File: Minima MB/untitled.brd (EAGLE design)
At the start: 101.3 x 130.5 mm, 224 parts, among them IC1 78L05, IC2 78L05, K1 G5V1, K2 G5V-2, K3 G5V1, K4 G5V1, Q10 2N3904, Q11 2N3904, Q12 2N3904, Q13 2N3904, Q14 2N3904, Q15 2N3904, Q16 2N3904, Q17 BFO, Q18 J310, Q19 J310, Q20 2N3904, Q21 2N3906, Q22 2N3904, Q23 2N3904, Q24 2N3904, Q25 2N3904, Q26 2N3904, Q27 2N3904, Q28 2N3904, Q29 2N3904, Q30 2N3904, Q39 2N3904, Q8 2N3904, X1 VFO, X2 VFO, X3 PA

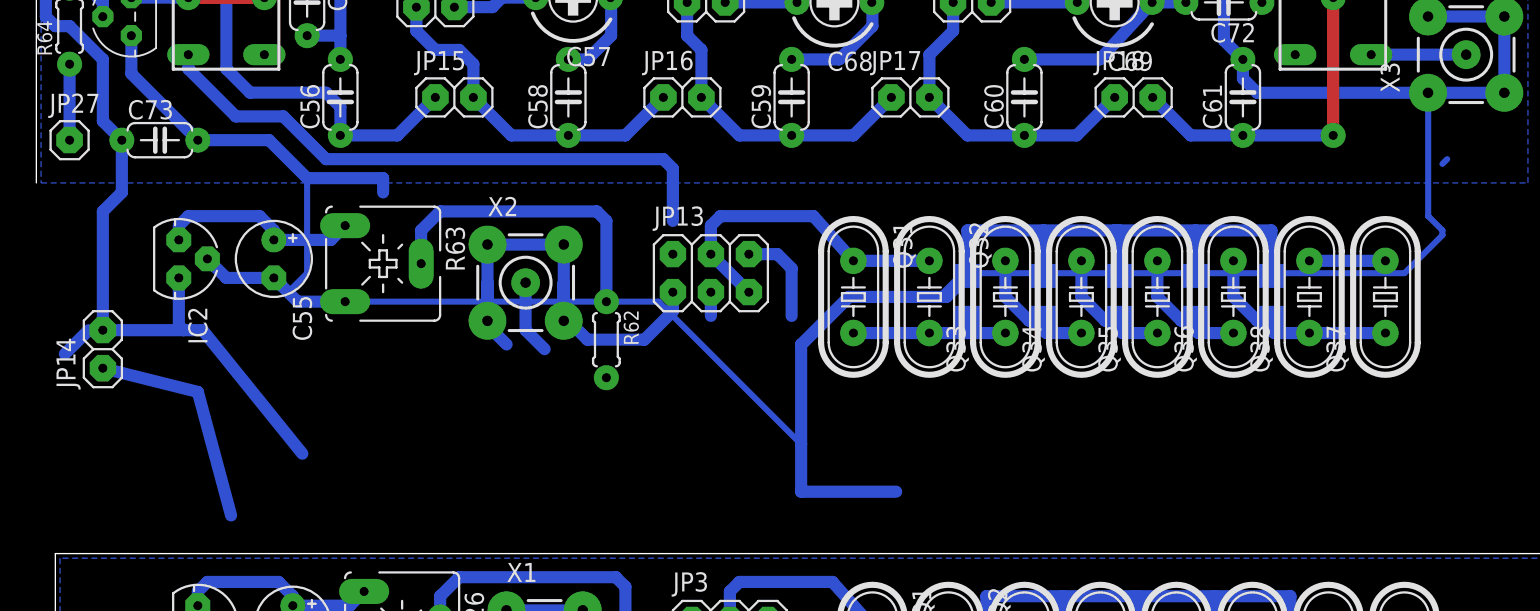
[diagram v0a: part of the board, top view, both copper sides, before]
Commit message: Deleted vestigle components, next I will shuffle the top half of the board back in to place.
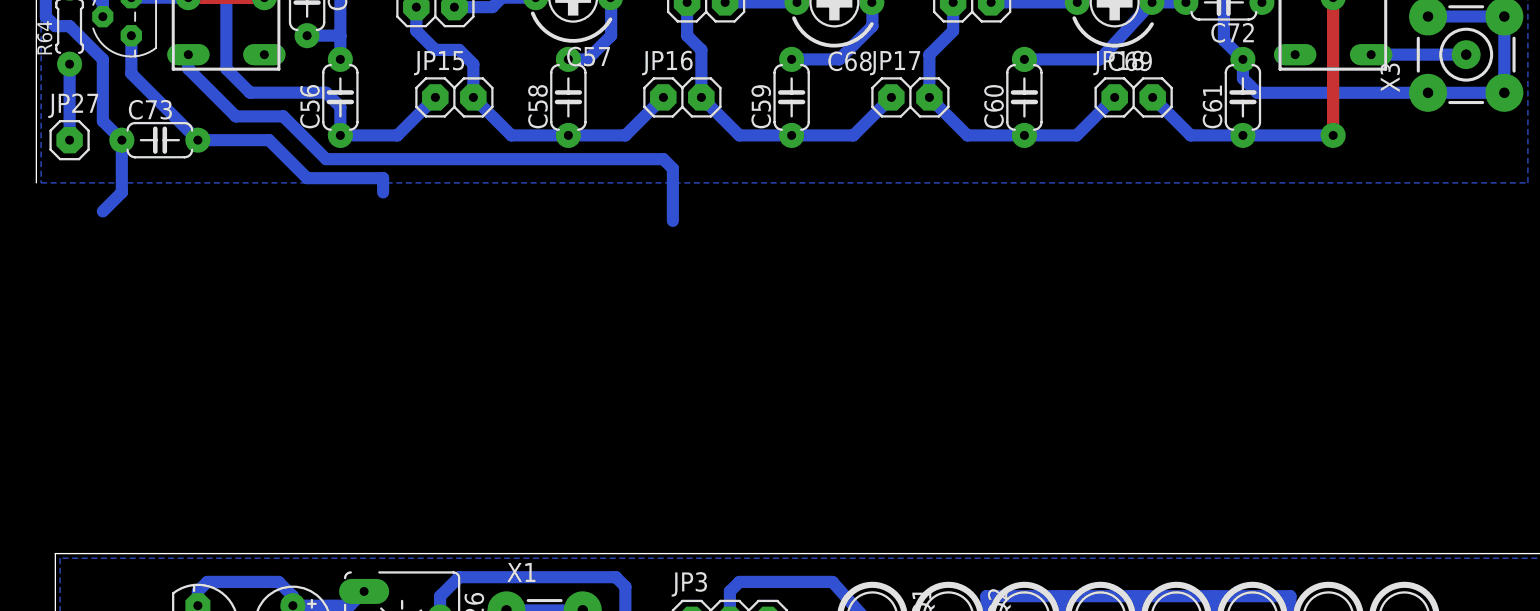
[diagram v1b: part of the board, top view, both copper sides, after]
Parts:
- removed C34, C51, C52, C53, C54: 100p, rcl:C1206
- removed C55: 50u, rcl:E2,5-5
- removed IC2: 78L05, v-reg:78LXX
- removed JP13: (no value), pinhead:2X03
- removed JP14: (no value), pinhead:1X02
- removed Q31, Q32, Q33, Q34, Q35, Q36, Q37, Q38: (no value), crystal:HC49/S
- removed R62: 4k7, rcl:0204/5
- removed R63: 10k, pot:CA6V
- removed X2: VFO, con-coax:BU-SMA-V
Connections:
- removed net 5VREG: C55.+, IC2.OUT, R63.A
- removed net N$100: X2.1
- removed net N$102: R62.1, R63.S
- removed net N$103: Q37.2, Q38.2
- removed net N$80: C34.1, Q31.2, Q32.2, Q33.1
- removed net N$88: C51.1, Q33.2, Q34.1
- removed net N$90: C52.1, Q34.2, Q35.1
- removed net N$92: C53.1, Q35.2, Q36.1
- removed net N$93: C54.1, Q36.2, Q37.1, Q38.1
- removed net N$94: JP13.4, JP13.5, Q31.1, Q32.1
- removed net N$95: JP13.3
- removed net N$96: JP13.6
- removed net N$97: R62.2
- net +12V: no longer IC2.IN, JP14.2
- net GND: no longer C34.2, C51.2, C52.2, C53.2, C54.2, C55.-, IC2.GND, JP13.1, JP14.1, R63.E, X2.2, X2.3, X2.4, X2.5
- net N$116: no longer JP13.2
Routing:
- net GND: track 1014.0 -> 783.3 mm
- net +12V: track 405.6 -> 374.5 mm
- net N$94: track 21.7 -> 0.00 mm
- net N$102: track 20.8 -> 0.00 mm
- net N$93: track 14.2 -> 0.00 mm
- net 5VREG: track 13.8 -> 0.00 mm
- net N$80: track 11.2 -> 0.00 mm
- net N$92: track 9.13 -> 0.00 mm
- net N$88: track 9.13 -> 0.00 mm
- net N$90: track 9.13 -> 0.00 mm
- net N$96: track 6.43 -> 0.00 mm
- net N$103: track 5.08 -> 0.00 mm
- net N$100: track 4.97 -> 0.00 mm
- net N$95: track 1.59 -> 0.00 mm

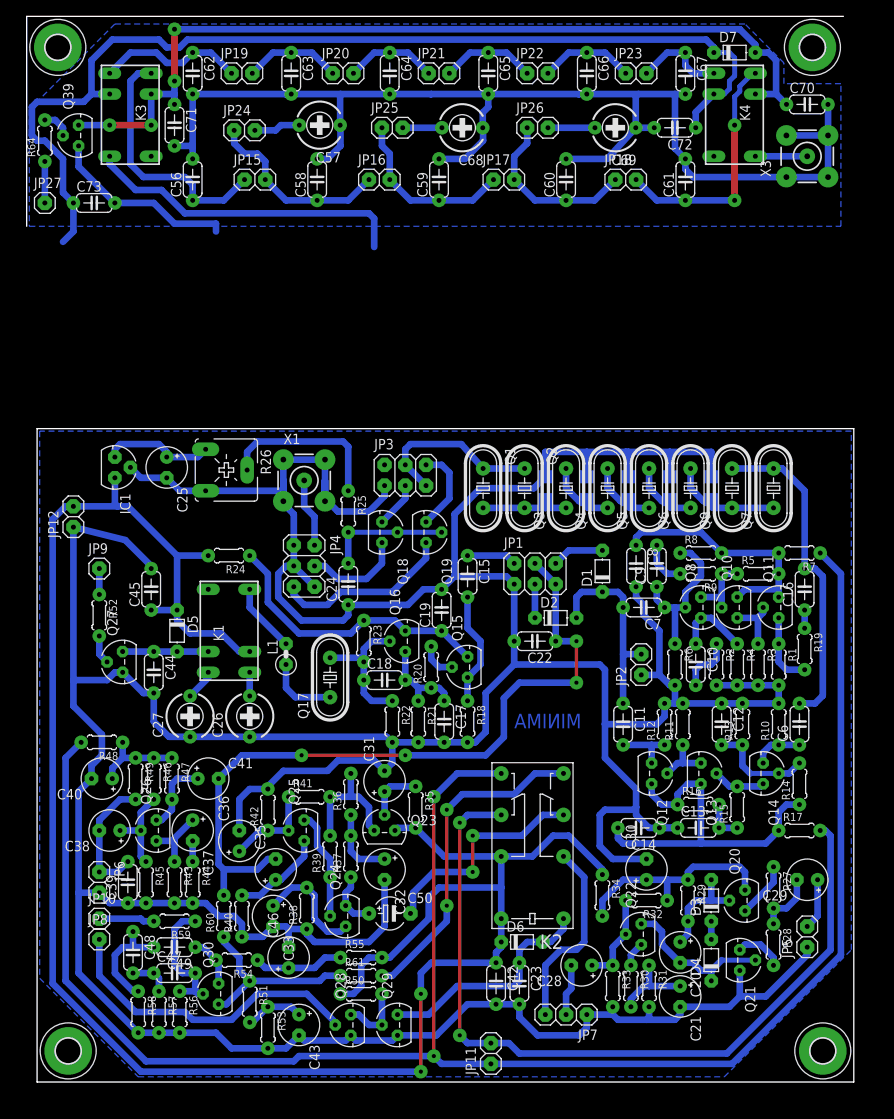
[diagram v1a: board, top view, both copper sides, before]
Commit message: Halves joined, airwires connected, board dimension fixed and GND fill poly redone and added a TOP layer GND fill.
Added BOMs as well.
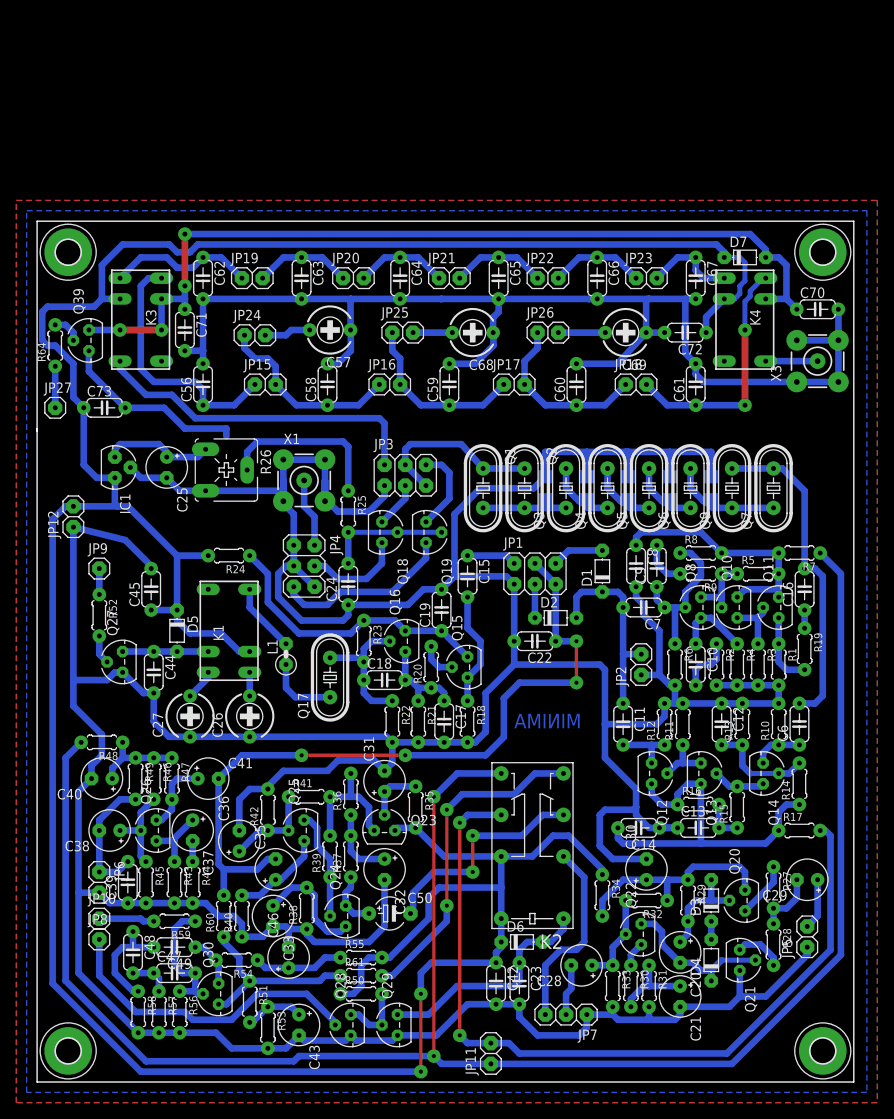
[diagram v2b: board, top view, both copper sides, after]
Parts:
- moved C68 25.1 mm to (53.3, 91.8)
- moved C69 25.1 mm to (72.1, 91.8)
- moved C70 25.1 mm to (95.6, 94.6)
- moved C72 25.1 mm to (79.4, 91.8)
- moved H3 25.1 mm to (3.81, 101.6)
- moved H4 25.1 mm to (96.2, 101.6)
- moved JP25 25.1 mm to (44.8, 91.8)
- moved JP26 25.1 mm to (62.5, 91.8)
- moved C56 25.1 mm to (20.3, 85.4)
- moved C57 25.1 mm to (35.9, 92.1)
- moved C58 25.1 mm to (35.6, 85.4)
- moved C59 25.1 mm to (50.5, 85.4)
- moved C60 25.1 mm to (66.0, 85.4)
- moved C61 25.1 mm to (80.6, 85.4)
- moved C62 25.1 mm to (20.3, 98.4)
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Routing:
- net +12V: track 374.5 -> 380.6 mm
- net N$116: track 39.6 -> 41.2 mm
- added copper zone on layer 1, net GND
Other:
- board size 101.3 x 130.5 mm -> 100 x 105.4 mm

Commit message: Added BOM files, remove unneeded files.
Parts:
- C50: value (none) -> 1 uF
- C57, C68, C69: value (none) -> 22 pF
- R14: value (none) -> 10k
- R48: value 10u -> 10
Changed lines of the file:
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@@
 <element name="R12" library="rcl" package="0204/5" value="220" x="76.835" y="43.815" rot="R90"/>
 <element name="C11" library="rcl" package="C050-024X044" value="0.1" x="71.755" y="43.815" rot="R270"/>
-<element name="R14" library="rcl" package="0204/5" value="" x="93.345" y="36.5125" rot="R90"/>
+<element name="R14" library="rcl" package="0204/5" value="10k" x="93.345" y="36.5125" rot="R90"/>
 <element name="R15" library="rcl" package="0204/5" value="470" x="85.725" y="33.655" rot="R90"/>
 <element name="R16" library="rcl" package="0204/5" value="4k7" x="80.9625" y="33.9725"/>
@@
 <element name="R46" library="rcl" package="0204/5" value="10k" x="14.2875" y="37.1475" rot="R270"/>
 <element name="R47" library="rcl" package="0204/5" value="1k" x="16.51" y="37.1475" rot="R270"/>
-<element name="R48" library="rcl" package="0204/5" value="10u" x="7.9375" y="41.5925" rot="R180"/>
+<element name="R48" library="rcl" package="0204/5" value="10" x="7.9375" y="41.5925" rot="R180"/>
 <element name="C38" library="rcl" package="E2,5-5" value="1u" x="8.89" y="30.7975" rot="R180"/>
 <element name="R49" library="rcl" package="0204/5" value="4k7" x="12.065" y="37.1475" rot="R270"/>
@@
 <element name="JP11" library="pinhead" package="1X02" value="" x="55.5625" y="3.4925" rot="R90"/>
 <element name="JP12" library="pinhead" package="1X02" value="" x="4.445" y="69.215" rot="R90"/>
-<element name="C50" library="rcl" package="E5-4" value="" x="43.18" y="20.6375"/>
+<element name="C50" library="rcl" package="E5-4" value="1 uF" x="43.18" y="20.6375"/>
 <element name="H1" library="holes" package="3,0-PAD" value="MOUNT-PAD-ROUND3.0" x="3.81" y="3.81"/>
 <element name="H2" library="holes" package="3,0-PAD" value="MOUNT-PAD-ROUND3.0" x="96.2025" y="3.81"/>
@@
 <element name="H4" library="holes" package="3,0-PAD" value="MOUNT-PAD-ROUND3.0" x="96.2025" y="101.6"/>
 <element name="C56" library="rcl" package="C050-024X044" value="" x="20.32" y="85.4075" rot="R90"/>
-<element name="C57" library="rcl" package="CTRIMTZ03" value="" x="35.8775" y="92.075" rot="R90"/>
+<element name="C57" library="rcl" package="CTRIMTZ03" value="22 pF" x="35.8775" y="92.075" rot="R90"/>
 <element name="JP15" library="pinhead" package="1X02" value="" x="27.94" y="85.4075"/>
 <element name="C58" library="rcl" package="C050-024X044" value="" x="35.56" y="85.4075" rot="R90"/>
@@
 <element name="JP25" library="pinhead" package="1X02" value="" x="44.7675" y="91.7575"/>
 <element name="JP26" library="pinhead" package="1X02" value="" x="62.5475" y="91.7575"/>
-<element name="C68" library="rcl" package="CTRIMTZ03" value="" x="53.34" y="91.7575" rot="R90"/>
-<element name="C69" library="rcl" package="CTRIMTZ03" value="" x="72.0725" y="91.7575" rot="R90"/>
+<element name="C68" library="rcl" package="CTRIMTZ03" value="22 pF" x="53.34" y="91.7575" rot="R90"/>
+<element name="C69" library="rcl" package="CTRIMTZ03" value="22 pF" x="72.0725" y="91.7575" rot="R90"/>
 <element name="Q39" library="transistor-npn" package="TO92" value="2N3904" x="6.35" y="90.805" rot="R90"/>
 <element name="R64" library="rcl" package="0204/5" value="4k7" x="2.2225" y="90.17" rot="R90"/>
